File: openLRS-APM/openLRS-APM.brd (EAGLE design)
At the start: 50 x 20 mm, 27 parts, among them IC1 MCP1703CB, IC2 RFM23BPSMD, J1 CON_HEADER_PRG_AVR_ICSP-SMD, Y1 16MHz

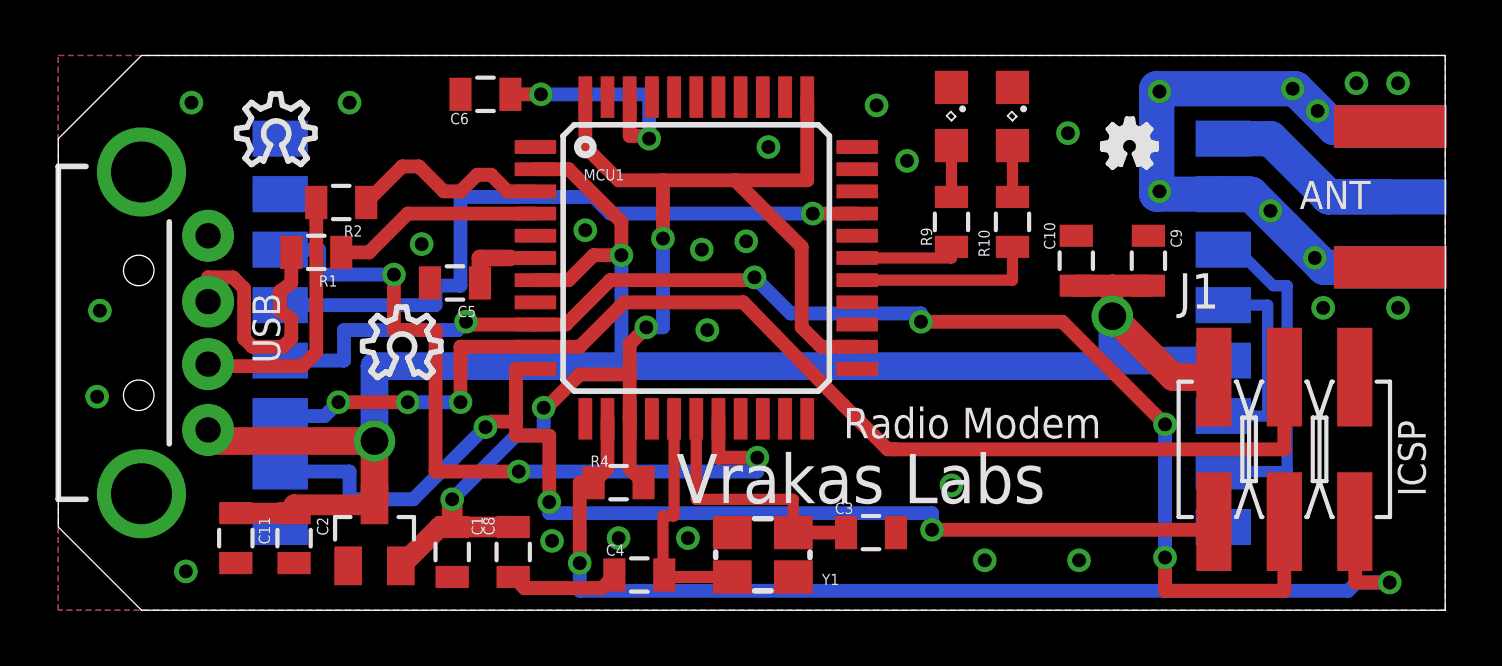
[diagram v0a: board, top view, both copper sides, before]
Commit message: Production Rev.1, changed the SMA connector.
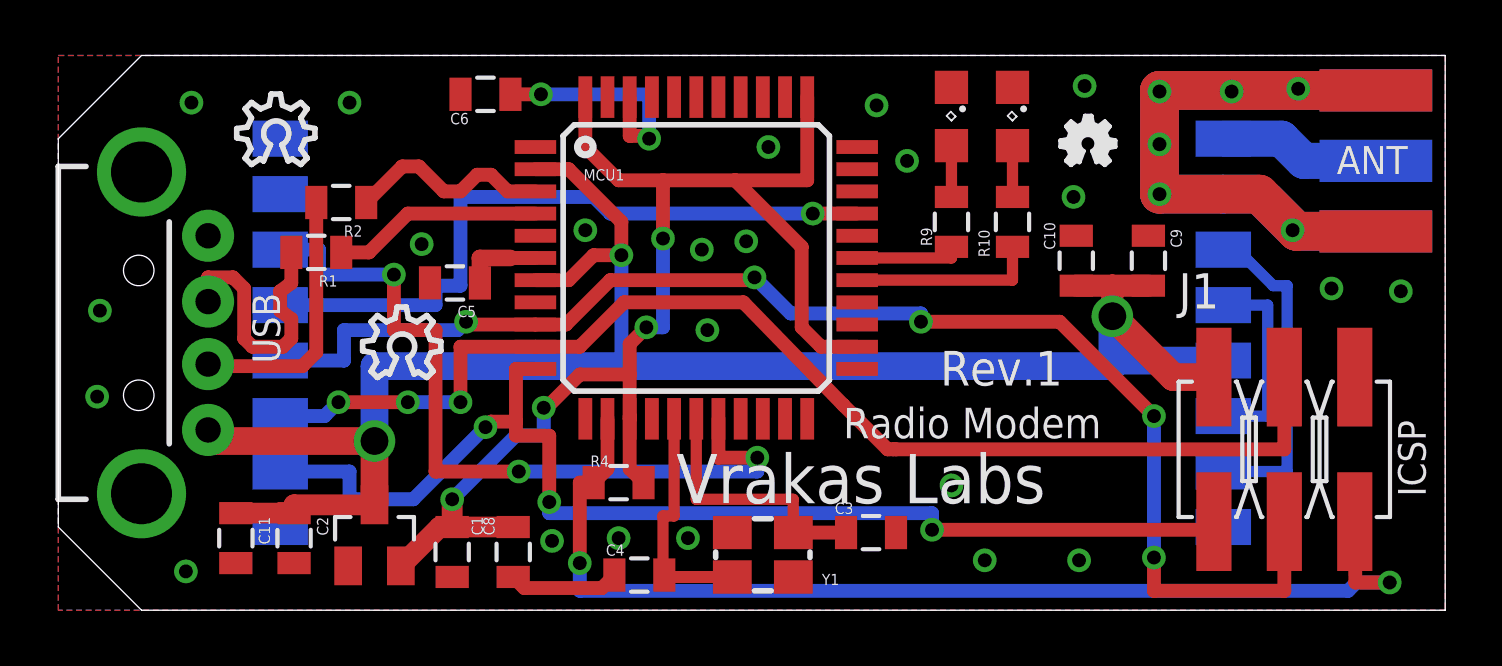
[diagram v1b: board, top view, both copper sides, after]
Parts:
- removed SMA: (no value), adafruit:SMA_EDGELAUNCH
- added U$4: LINX-SMA, OpenLRS-APM:LINX-SMA
- moved U$1 1.50 mm to (36.1, 16.0)
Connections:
- net GND: now also U$4.GND1, U$4.GND2, U$4.GND3, U$4.GND4; no longer SMA.GND@1, SMA.GND@2, SMA.GND@3, SMA.GND@4
- net N$13: now also U$4.RF; no longer SMA.P
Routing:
- net GND: track 26.4 -> 43.5 mm, vias 30 -> 29
- net N$13: track 6.89 -> 5.83 mm
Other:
- board text added: "Rev.1"
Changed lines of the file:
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@@
 <?xml version="1.0" encoding="utf-8"?>
 <!DOCTYPE eagle SYSTEM "eagle.dtd">
-<eagle version="7.1.0">
+<eagle version="7.2.0">
 <drawing>
 <settings>
@@
 <setting verticaltext="up"/>
 </settings>
-<grid distance="0.1" unitdist="mm" unit="mm" style="lines" multiple="1" display="no" altdistance="0.025" altunitdist="inch" altunit="inch"/>
+<grid distance="0.1" unitdist="mm" unit="mm" style="lines" multiple="1" display="no" altdistance="0.1" altunitdist="mm" altunit="mm"/>
 <layers>
 <layer number="1" name="Top" color="4" fill="1" visible="yes" active="yes"/>
@@
 <layer number="56" name="wert" color="7" fill="1" visible="no" active="no"/>
 <layer number="57" name="tCAD" color="7" fill="1" visible="no" active="no"/>
+<layer number="90" name="Modules" color="5" fill="1" visible="no" active="no"/>
 <layer number="91" name="Nets" color="2" fill="1" visible="no" active="no"/>
 <layer number="92" name="Busses" color="1" fill="1" visible="no" active="no"/>
@@
 <wire x1="50" y1="20" x2="3" y2="20" width="0" layer="20"/>
 <wire x1="50" y1="0" x2="50" y2="20" width="0" layer="20"/>
-<text x="44.751" y="14.465" size="1.016" layer="25">ANT</text>
+<text x="48.649" y="16.735" size="1.016" layer="25" rot="R180">ANT</text>
 <text x="22.277" y="3.856" size="1.778" layer="21" font="vector">Vrakas Labs</text>
 <text x="28.3" y="6.2" size="1.1" layer="21" font="vector">Radio Modem</text>
 <text x="49.3" y="4.1" size="1" layer="21" rot="R90">ICSP</text>
 <text x="8" y="8.9" size="1" layer="21" rot="R90">USB</text>
+<text x="31.8" y="8.1" size="1.25" layer="21">Rev.1</text>
 </plain>
 <attributes>
@@
 <attribute name="VALUE" x="15.354" y="17.484" size="0.4064" layer="27"/>
 </element>
-<element name="SMA" library="adafruit" package="SMA_EDGELAUNCH" value=" " x="50.053" y="14.9" smashed="yes" rot="MR0"/>
-<element name="U$1" library="ohw-logo" package="OSHW_FILLX70_NOTEXT" value="" x="37.629" y="15.949"/>
+<element name="U$1" library="ohw-logo" package="OSHW_FILLX70_NOTEXT" value="" x="36.129" y="16.049"/>
 <element name="U$2" library="ohw-logo" package="OSHW_8X100_NOTEXT" value="" x="6.432" y="16.07"/>
 <element name="U$3" library="ohw-logo" package="OSHW_8X100_NOTEXT" value="" x="10.972" y="8.39"/>
@@
 <element name="C5" library="SparkFun-Capacitors" package="0805" value="1uF" x="14.3" y="11.8" rot="R180"/>
 <element name="J1" library="dp_devices" package="M2X3_SMD" value="CON_HEADER_PRG_AVR_ICSP-SMD" x="44.2" y="5.8"/>
+<element name="U$4" library="OpenLRS-APM" package="LINX-SMA" value="LINX-SMA" x="47.5" y="16.2" rot="MR180"/>
 </elements>
 <signals>
@@
 <vertex x="0" y="20"/>
 </polygon>
-<contactref element="SMA" pad="GND@1"/>
-<contactref element="SMA" pad="GND@3"/>
-<contactref element="SMA" pad="GND@4"/>
-<contactref element="SMA" pad="GND@2"/>
 <contactref element="IC1" pad="1"/>
 <contactref element="C1" pad="2"/>
@@
 <via x="13.1" y="13.2" extent="1-16" drill="0.5"/>
 <via x="24.8" y="13.3" extent="1-16" drill="0.5"/>
-<via x="36.4" y="17.2" extent="1-16" drill="0.5"/>
+<via x="37" y="18.9" extent="1-16" drill="0.5"/>
 <via x="32.2" y="4.5" extent="1-16" drill="0.5"/>
 <via x="22.7" y="2.6" extent="1-16" drill="0.5"/>
@@
 <via x="1.5" y="10.8" extent="1-16" drill="0.5"/>
 <via x="1.4" y="7.7" extent="1-16" drill="0.5"/>
-<via x="39.7" y="15.1" extent="1-16" drill="0.5"/>
+<via x="39.7" y="15" extent="1-16" drill="0.5"/>
 <via x="36.8" y="1.8" extent="1-16" drill="0.5"/>
 <via x="33.4" y="1.8" extent="1-16" drill="0.5"/>
@@
 <via x="23.2" y="13" extent="1-16" drill="0.5"/>
 <via x="23.4" y="10.1" extent="1-16" drill="0.5"/>
-<via x="48.3" y="19" extent="1-16" drill="0.5"/>
-<via x="48.3" y="10.9" extent="1-16" drill="0.5"/>
-<via x="45.6" y="10.9" extent="1-16" drill="0.5"/>
-<via x="44.5" y="18.8" extent="1-16" drill="0.5"/>
-<wire x1="42" y1="15" x2="43" y2="15" width="1.27" layer="16"/>
-<wire x1="43" y1="15" x2="45.64" y2="12.36" width="1.27" layer="16"/>
-<wire x1="45.64" y1="12.36" x2="48.021" y2="12.36" width="1.27" layer="16"/>
-<wire x1="42" y1="15" x2="39.6" y2="15" width="1.27" layer="16"/>
-<wire x1="39.6" y1="15" x2="39.6" y2="18.8" width="1.27" layer="16"/>
-<wire x1="39.6" y1="18.8" x2="44.6" y2="18.8" width="1.27" layer="16"/>
-<wire x1="44.6" y1="18.8" x2="46" y2="17.4" width="1.27" layer="16"/>
-<wire x1="46" y1="17.4" x2="47.981" y2="17.4" width="1.27" layer="16"/>
-<wire x1="47.981" y1="17.4" x2="48.021" y2="17.44" width="1.27" layer="16"/>
+<via x="48.4" y="11.5" extent="1-16" drill="0.5"/>
+<via x="39.7" y="16.8" extent="1-16" drill="0.5"/>
+<via x="42.3" y="18.7" extent="1-16" drill="0.5"/>
+<via x="44.7" y="18.8" extent="1-16" drill="0.5"/>
 <polygon width="0.4064" layer="16">
 <vertex x="50" y="20"/>
@@
 <vertex x="0" y="20"/>
 </polygon>
-<via x="45.4" y="18" extent="1-16" drill="0.5"/>
-<via x="45.3" y="12.7" extent="1-16" drill="0.5"/>
-<via x="43.7" y="14.4" extent="1-16" drill="0.5"/>
+<via x="45.9" y="11.6" extent="1-16" drill="0.5"/>
+<via x="44.5" y="13.7" extent="1-16" drill="0.5"/>
+<via x="36.6" y="14.9" extent="1-16" drill="0.5"/>
 <via x="39.7" y="18.7" extent="1-16" drill="0.5"/>
-<via x="46.8" y="19" extent="1-16" drill="0.5"/>
+<contactref element="U$4" pad="GND2"/>
+<contactref element="U$4" pad="GND3"/>
+<contactref element="U$4" pad="GND4"/>
+<contactref element="U$4" pad="GND1"/>
+<wire x1="47.5" y1="18.74" x2="39.7" y2="18.74" width="1.4" layer="16"/>
+<wire x1="39.7" y1="18.74" x2="39.7" y2="15" width="1.4" layer="16"/>
+<wire x1="39.7" y1="15" x2="42" y2="15" width="1.4" layer="16"/>
+<wire x1="42" y1="15" x2="43.3" y2="15" width="1.4" layer="16"/>
+<wire x1="47.5" y1="18.74" x2="39.7" y2="18.74" width="1.4" layer="1"/>
+<wire x1="39.7" y1="18.74" x2="39.7" y2="18.7" width="1.4" layer="1"/>
+<wire x1="39.7" y1="18.7" x2="39.7" y2="15" width="1.4" layer="1"/>
+<wire x1="39.7" y1="15" x2="43.3" y2="15" width="1.4" layer="1"/>
+<wire x1="43.3" y1="15" x2="44.64" y2="13.66" width="1.4" layer="1"/>
+<wire x1="44.64" y1="13.66" x2="47.5" y2="13.66" width="1.4" layer="1"/>
+<wire x1="47.5" y1="13.66" x2="44.64" y2="13.66" width="1.4" layer="16"/>
+<wire x1="44.64" y1="13.66" x2="43.5" y2="14.8" width="1.4" layer="16"/>
 </signal>
 <signal name="/RESET">
@@
 <contactref element="J1" pad="3"/>
 <wire x1="44.2" y1="3.195" x2="44.2" y2="0.7" width="0.5" layer="1"/>
-<wire x1="44.2" y1="0.7" x2="39.9" y2="0.7" width="0.5" layer="1"/>
+<wire x1="44.2" y1="0.7" x2="39.5" y2="0.7" width="0.5" layer="1"/>
 <wire x1="8" y1="9" x2="10.3" y2="9" width="0.5" layer="16"/>
 <wire x1="10.3" y1="9" x2="10.3" y2="10.1" width="0.5" layer="16"/>
@@
 <wire x1="14.7" y1="10.4" x2="14.7" y2="10.3" width="0.5" layer="1"/>
 <wire x1="14.7" y1="10.3" x2="17.2" y2="10.3" width="0.5" layer="1"/>
-<wire x1="39.9" y1="0.7" x2="39.9" y2="1.9" width="0.5" layer="1"/>
-<via x="39.9" y="1.9" extent="1-16" drill="0.5"/>
-<wire x1="39.9" y1="1.9" x2="39.9" y2="6.7" width="0.5" layer="16"/>
-<via x="39.9" y="6.7" extent="1-16" drill="0.5"/>
-<wire x1="39.9" y1="6.7" x2="36.2" y2="10.4" width="0.5" layer="1"/>
-<wire x1="36.2" y1="10.4" x2="31.1" y2="10.4" width="0.5" layer="1"/>
+<wire x1="39.5" y1="0.7" x2="39.5" y2="1.9" width="0.5" layer="1"/>
+<via x="39.5" y="1.9" extent="1-16" drill="0.5"/>
+<wire x1="39.5" y1="1.9" x2="39.5" y2="7" width="0.5" layer="16"/>
+<via x="39.5" y="7" extent="1-16" drill="0.5"/>
+<wire x1="39.5" y1="7" x2="36.1" y2="10.4" width="0.5" layer="1"/>
+<wire x1="36.1" y1="10.4" x2="31.1" y2="10.4" width="0.5" layer="1"/>
 <via x="31.1" y="10.4" extent="1-16" drill="0.5"/>
 <wire x1="31.1" y1="10.4" x2="31.1" y2="10.7" width="0.5" layer="16"/>
@@
 <signal name="N$13">
 <contactref element="IC2" pad="1"/>
-<contactref element="SMA" pad="P"/>
-<wire x1="48.021" y1="14.9" x2="45.8" y2="14.9" width="1.27" layer="16"/>
-<wire x1="45.8" y1="14.9" x2="43.7" y2="17" width="1.27" layer="16"/>
-<wire x1="43.7" y1="17" x2="42" y2="17" width="1.27" layer="16"/>
+<contactref element="U$4" pad="RF"/>
+<wire x1="42" y1="17" x2="44.1" y2="17" width="1.3" layer="16"/>
+<wire x1="44.1" y1="17" x2="44.9" y2="16.2" width="1.3" layer="16"/>
+<wire x1="44.9" y1="16.2" x2="47.5" y2="16.2" width="1.3" layer="16"/>
 </signal>
 <signal name="N$24">
